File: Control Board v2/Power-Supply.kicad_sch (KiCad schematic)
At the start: 12 parts, among them J1 1366005, J6 Conn_01x04, SW1 SW_SPST

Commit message: got most HV routed
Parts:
- F1: footprint Fuse:Fuse_Blade_ATO_directSolder -> Fuse:Fuseholder_Clip-5x20mm_Bel_FC-203-22_Lateral_P17.80x5.00mm_D1.17mm_Horizontal
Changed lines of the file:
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@@
 			)
 		)
-		(property "Footprint" "Fuse:Fuse_Blade_ATO_directSolder"
+		(property "Footprint" "Fuse:Fuseholder_Clip-5x20mm_Bel_FC-203-22_Lateral_P17.80x5.00mm_D1.17mm_Horizontal"
 			(at 162.56 135.128 90)
 			(effects

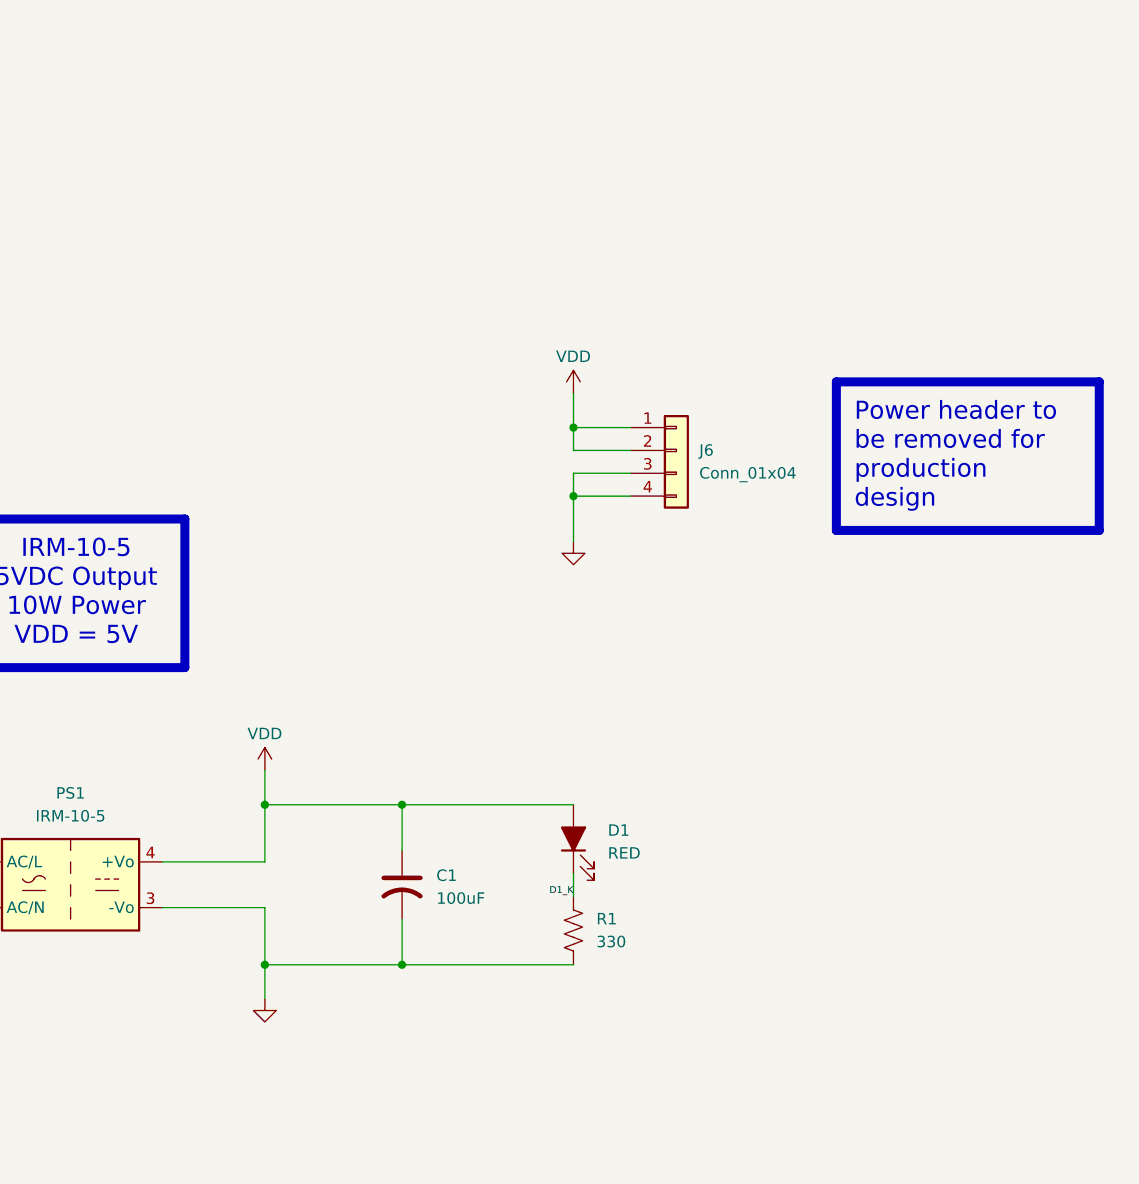
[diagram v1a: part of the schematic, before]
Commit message: add external 5v input and move stuff around on board
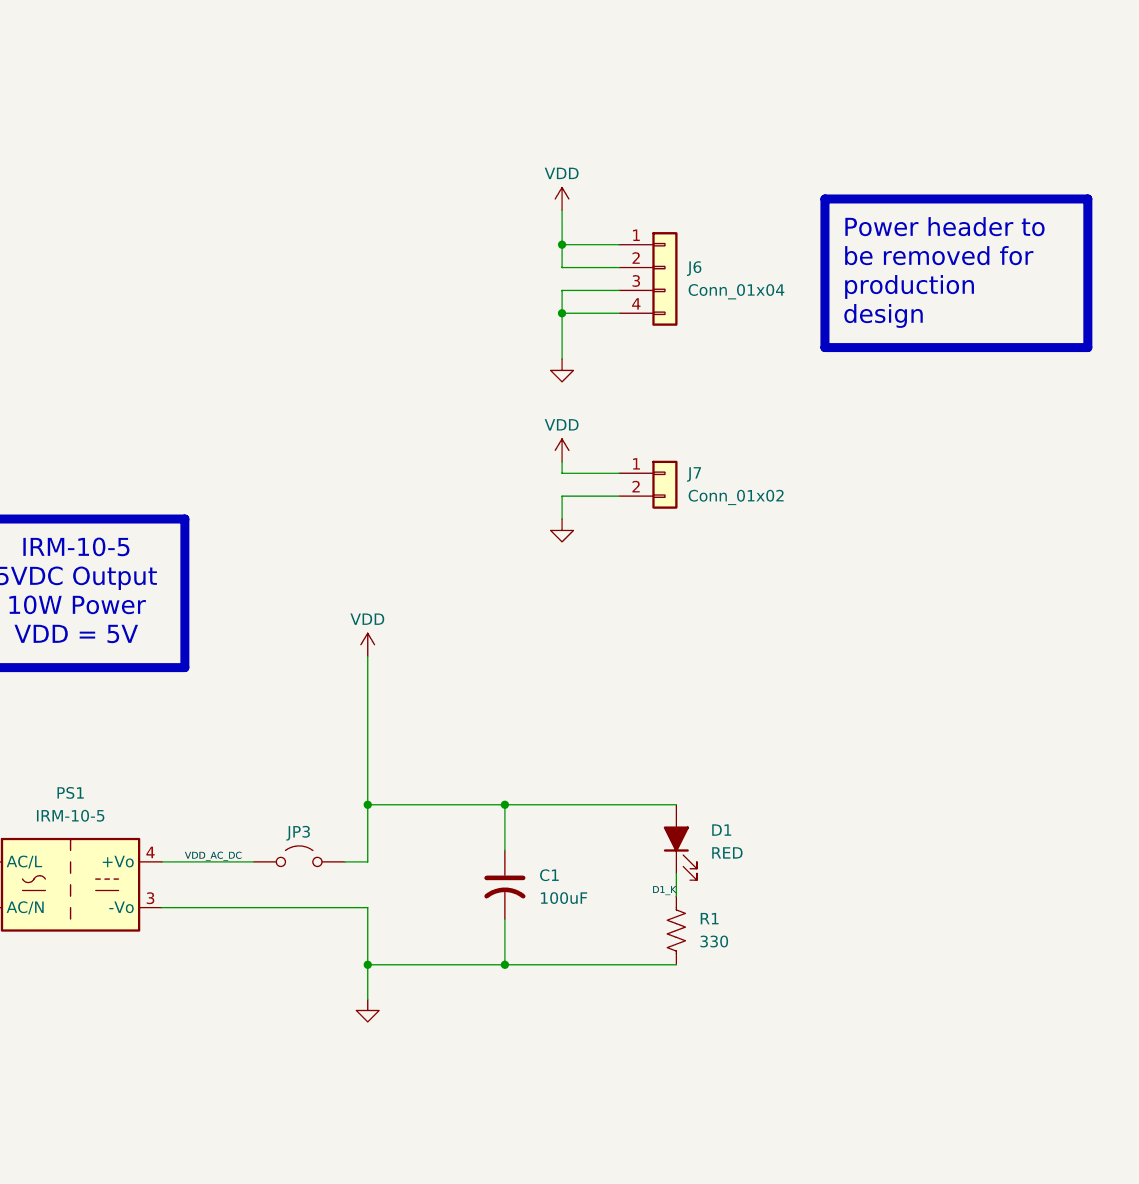
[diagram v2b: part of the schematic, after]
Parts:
- added J7: Conn_01x02, TerminalBlock_Phoenix:TerminalBlock_Phoenix_MKDS-1,5-2-5.08_1x02_P5.08mm_Horizontal, symbol Connector_Generic:Conn_01x02
- added JP3: Jumper_2_Open, Connector_PinHeader_2.54mm:PinHeader_1x02_P2.54mm_Vertical, symbol Jumper:Jumper_2_Open
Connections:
- net GND: now also J7.2 (Pin_2)
- net VDD: now also J7.1 (Pin_1), JP3.2 (B); no longer PS1.4 (+Vo)
- new net VDD_AC_DC: JP3.1 (A), PS1.4 (+Vo)
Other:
- moved on the sheet: C1, D1, J6, R1
